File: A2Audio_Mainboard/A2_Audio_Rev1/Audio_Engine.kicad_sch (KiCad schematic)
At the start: 22 parts, among them U10 OPA1622IDRCR, U6 U_DAC_L, U7 U_DAC_R, U8 TPS7A2018PDBVR, U9 TPS7A2033PDBVR

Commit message: Added footprints and a few more parts.
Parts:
- C10, C100, C101, C102, C11, C12, C13, C14, C15, C7, C8, C9, C95, C96, C97, C98, C99: footprint (none) -> Capacitor_SMD:C_0402_1005Metric
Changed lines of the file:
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@@
 			)
 		)
-		(property "Footprint" ""
+		(property "Footprint" "Capacitor_SMD:C_0402_1005Metric"
 			(at 133.0452 99.06 0)
 			(hide yes)
@@
 			)
 		)
-		(property "Footprint" ""
+		(property "Footprint" "Capacitor_SMD:C_0402_1005Metric"
 			(at 179.07 56.1848 0)
 			(hide yes)
@@
 			)
 		)
-		(property "Footprint" ""
+		(property "Footprint" "Capacitor_SMD:C_0402_1005Metric"
 			(at 218.1352 186.69 0)
 			(hide yes)
@@
 			)
 		)
-		(property "Footprint" ""
+		(property "Footprint" "Capacitor_SMD:C_0402_1005Metric"
 			(at 28.9052 73.66 0)
 			(hide yes)
@@
 			)
 		)
-		(property "Footprint" ""
+		(property "Footprint" "Capacitor_SMD:C_0402_1005Metric"
 			(at 120.3452 97.79 0)
 			(hide yes)
@@
 			)
 		)
-		(property "Footprint" ""
+		(property "Footprint" "Capacitor_SMD:C_0402_1005Metric"
 			(at 34.29 29.5148 0)
 			(hide yes)
@@
 			)
 		)
-		(property "Footprint" ""
+		(property "Footprint" "Capacitor_SMD:C_0402_1005Metric"
 			(at 263.8552 97.79 0)
 			(hide yes)
@@
 			)
 		)
-		(property "Footprint" ""
+		(property "Footprint" "Capacitor_SMD:C_0402_1005Metric"
 			(at 36.5252 87.63 0)
 			(hide yes)
@@
 			)
 		)
-		(property "Footprint" ""
+		(property "Footprint" "Capacitor_SMD:C_0402_1005Metric"
 			(at 113.9952 102.87 0)
 			(hide yes)
@@
 			)
 		)
-		(property "Footprint" ""
+		(property "Footprint" "Capacitor_SMD:C_0402_1005Metric"
 			(at 33.02 56.1848 0)
 			(hide yes)
@@
 			)
 		)
-		(property "Footprint" ""
+		(property "Footprint" "Capacitor_SMD:C_0402_1005Metric"
 			(at 169.8752 85.09 0)
 			(hide yes)
@@
 			)
 		)
-		(property "Footprint" ""
+		(property "Footprint" "Capacitor_SMD:C_0402_1005Metric"
 			(at 203.5048 115.57 0)
 			(hide yes)
@@
 			)
 		)
-		(property "Footprint" ""
+		(property "Footprint" "Capacitor_SMD:C_0402_1005Metric"
 			(at 276.5552 99.06 0)
 			(hide yes)
@@
 			)
 		)
-		(property "Footprint" ""
+		(property "Footprint" "Capacitor_SMD:C_0402_1005Metric"
 			(at 257.5052 105.41 0)
 			(hide yes)
@@
 			)
 		)
-		(property "Footprint" ""
+		(property "Footprint" "Capacitor_SMD:C_0402_1005Metric"
 			(at 263.1948 113.03 0)
 			(hide yes)
@@
 			)
 		)
-		(property "Footprint" ""
+		(property "Footprint" "Capacitor_SMD:C_0402_1005Metric"
 			(at 180.0352 87.63 0)
 			(hide yes)
@@
 			)
 		)
-		(property "Footprint" ""
+		(property "Footprint" "Capacitor_SMD:C_0402_1005Metric"
 			(at 177.8 34.5948 0)
 			(hide yes)

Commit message: Refining of logic and adding battery connector
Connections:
- net 1V8_DIG: no longer C9.1, U10.8 (EN), U6.25 (VCP), U6.26 (VP), U6.31 (VL), U6.7 (VA), U7.25 (VCP), U7.26 (VP), U7.30 (ADR), U7.31 (VL), U7.7 (VA), U9.5 (OUT)
- new net 3V3_ANA: C9.1, U10.8 (EN), U6.25 (VCP), U6.26 (VP), U6.31 (VL), U6.7 (VA), U7.25 (VCP), U7.26 (VP), U7.30 (ADR), U7.31 (VL), U7.7 (VA), U9.5 (OUT)
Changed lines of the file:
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@@
-	)
-	(junction
-		(at 267.97 77.47)
-		(diameter 0)
-		(color 0 0 0 0)
 	)
 	(junction
@@
 	(wire
 		(pts
-			(xy 251.46 77.47) (xy 267.97 77.47)
-		)
-		(stroke
-			(width 0)
-			(type default)
-		)
-	)
-	(wire
-		(pts
 			(xy 410.21 130.81) (xy 417.83 130.81)
 		)
@@
 	(wire
 		(pts
+			(xy 251.46 77.47) (xy 255.27 77.47)
+		)
+		(stroke
+			(width 0)
+			(type default)
+		)
+	)
+	(wire
+		(pts
 			(xy 107.95 49.53) (xy 154.94 49.53)
 		)
@@
 	(wire
 		(pts
-			(xy 267.97 77.47) (xy 267.97 82.55)
-		)
-		(stroke
-			(width 0)
-			(type default)
-		)
-	)
-	(wire
-		(pts
 			(xy 185.42 40.64) (xy 185.42 35.56)
 		)
@@
 	(wire
 		(pts
-			(xy 267.97 76.2) (xy 267.97 77.47)
-		)
-		(stroke
+			(xy 267.97 76.2) (xy 267.97 82.55)
+		)
+		(stroke

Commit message: Fixing ERC errors
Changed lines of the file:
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@@
-		)
-	)
-	(wire
-		(pts
-			(xy 361.95 138.43) (xy 361.95 139.7)
-		)
-		(stroke
-			(width 0)
-			(type default)
 		)
 	)
@@
 	)
 	(label "3V3_ANA"
-		(at 271.78 76.2 0)
+		(at 284.48 76.2 0)
 		(effects
 			(font
@@
 	)
 	(label "AUDIO_OUT_L"
-		(at 359.41 125.73 0)
+		(at 356.87 125.73 0)
 		(effects
 			(font
@@
 	)
 	(label "AUDIO_OUT_R"
-		(at 359.41 133.35 0)
+		(at 356.87 133.35 0)
 		(effects
 			(font
@@
 	)
 	(label "3V3_ANA"
-		(at 119.38 95.25 0)
+		(at 130.81 95.25 0)
 		(effects
 			(font
@@
 	)
 	(label "3V3_ANA"
-		(at 364.49 138.43 0)
+		(at 361.95 138.43 0)
 		(effects
 			(font
@@
 	)
 	(label "1V8_DIG"
-		(at 111.76 77.47 0)
+		(at 124.46 77.47 0)
 		(effects
 			(font

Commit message: Fixed even more schematic errors
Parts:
- added R19, R31: 4.7kΩ, Resistor_SMD:R_0402_1005Metric, symbol symbols:R
- C10, C13: value 2.2µF -> 4.7µF
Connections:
- net 3V3_ANA: now also R19.2, R31.2
- net I2C_DAC_SCL: now also R19.1
- net I2C_DAC_SDA: now also R31.1
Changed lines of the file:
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@@
 	)
 	(junction
+		(at 153.67 111.76)
+		(diameter 0)
+		(color 0 0 0 0)
+	)
+	(junction
 		(at 260.35 71.12)
 		(diameter 0)
@@
 	)
 	(junction
+		(at 144.78 49.53)
+		(diameter 0)
+		(color 0 0 0 0)
+	)
+	(junction
 		(at 185.42 64.77)
 		(diameter 0)
@@
 	(wire
 		(pts
+			(xy 134.62 121.92) (xy 153.67 121.92)
+		)
+		(stroke
+			(width 0)
+			(type default)
+		)
+	)
+	(wire
+		(pts
 			(xy 154.94 31.75) (xy 257.81 31.75)
 		)
@@
 	(wire
 		(pts
+			(xy 144.78 49.53) (xy 144.78 123.19)
+		)
+		(stroke
+			(width 0)
+			(type default)
+		)
+	)
+	(wire
+		(pts
 			(xy 203.2 157.48) (xy 203.2 190.5)
 		)
@@
 	(wire
 		(pts
-			(xy 107.95 49.53) (xy 154.94 49.53)
+			(xy 107.95 49.53) (xy 144.78 49.53)
 		)
 		(stroke
@@
 	(wire
 		(pts
-			(xy 24.13 111.76) (xy 158.75 111.76)
+			(xy 24.13 111.76) (xy 153.67 111.76)
 		)
 		(stroke
@@
 	(wire
 		(pts
+			(xy 153.67 121.92) (xy 153.67 111.76)
+		)
+		(stroke
+			(width 0)
+			(type default)
+		)
+	)
+	(wire
+		(pts
 			(xy 161.29 35.56) (xy 170.18 35.56)
 		)
@@
 	(wire
 		(pts
+			(xy 144.78 49.53) (xy 154.94 49.53)
+		)
+		(stroke
+			(width 0)
+			(type default)
+		)
+	)
+	(wire
+		(pts
 			(xy 171.45 58.42) (xy 184.15 58.42)
 		)
@@
 	(wire
 		(pts
+			(xy 153.67 111.76) (xy 158.75 111.76)
+		)
+		(stroke
+			(width 0)
+			(type default)
+		)
+	)
+	(wire
+		(pts
 			(xy 185.42 67.31) (xy 182.88 67.31)
 		)
@@
 		)
 	)
+	(label "3V3_ANA"
+		(at 134.62 129.54 0)
+		(effects
+			(font
+				(size 1.27 1.27)
+			)
+			(justify left bottom)
+		)
+	)
 	(label "1V8_DIG"
 		(at 255.27 77.47 0)
@@
 		)
 	)
+	(label "3V3_ANA"
+		(at 144.78 130.81 270)
+		(effects
+			(font
+				(size 1.27 1.27)
+			)
+			(justify right bottom)
+		)
+	)
 	(label "1V8_DIG"
 		(at 124.46 77.47 0)
@@
 			)
 		)
-		(property "Value" "2.2µF"
+		(property "Value" "4.7µF"
 			(at 30.48 25.4 90)
 			(show_name no)
@@
 	)
 	(symbol
+		(lib_id "symbols:R")
+		(at 144.78 127 0)
+		(unit 1)
+		(body_style 1)
+		(exclude_from_sim no)
+		(in_bom yes)
+		(on_board yes)
+		(in_pos_files yes)
+		(dnp no)
+		(fields_autoplaced yes)
+		(property "Reference" "R31"
+			(at 147.32 125.7299 0)
+			(show_name no)
+			(do_not_autoplace no)
+			(effects
+				(font
+					(size 1.27 1.27)
+				)
+				(justify left)
+			)
+		)
+		(property "Value" "4.7kΩ"
+			(at 147.32 128.2699 0)
+			(show_name no)
+			(do_not_autoplace no)
+			(effects
+				(font
+					(size 1.27 1.27)
+				)
+				(justify left)
+			)
+		)
+		(property "Footprint" "Resistor_SMD:R_0402_1005Metric"
+			(at 143.002 127 90)
+			(hide yes)
+			(show_name no)
+			(do_not_autoplace no)
+			(effects
+				(font
+					(size 1.27 1.27)
+				)
+			)
+		)
+		(property "Datasheet" ""
+			(at 144.78 127 0)
+			(hide yes)
+			(show_name no)
+			(do_not_autoplace no)
+			(effects
+				(font
+					(size 1.27 1.27)
+				)
+			)
+		)
+		(property "Description" "Resistor"
+			(at 144.78 127 0)
+			(hide yes)
+			(show_name no)
+			(do_not_autoplace no)
+			(effects
+				(font
+					(size 1.27 1.27)
+				)
+			)
+		)
+		(pin "1"
+		)
+		(pin "2"
+		)
+		(instances
+			(project "A2_Audio_Rev1"
+				(path "/6bc02254-56bf-4f9a-8c1a-77c700c92092/966fe543-f3f2-44f2-9a96-3d2890d0362e"
+					(reference "R31")
+					(unit 1)
+				)
+			)
+		)
+	)
+	(symbol
 		(lib_id "symbols:GND")
 		(at 168.91 85.09 0)
@@
 	)
 	(symbol
+		(lib_id "symbols:R")
+		(at 134.62 125.73 0)
+		(unit 1)
+		(body_style 1)
+		(exclude_from_sim no)
+		(in_bom yes)
+		(on_board yes)
+		(in_pos_files yes)
+		(dnp no)
+		(fields_autoplaced yes)
+		(property "Reference" "R19"
+			(at 137.16 124.4599 0)
+			(show_name no)
+			(do_not_autoplace no)
+			(effects
+				(font
+					(size 1.27 1.27)
+				)
+				(justify left)
+			)
+		)
+		(property "Value" "4.7kΩ"
+			(at 137.16 126.9999 0)
+			(show_name no)
+			(do_not_autoplace no)
+			(effects
+				(font
+					(size 1.27 1.27)
+				)
+				(justify left)
+			)
+		)
+		(property "Footprint" "Resistor_SMD:R_0402_1005Metric"
+			(at 132.842 125.73 90)
+			(hide yes)
+			(show_name no)
+			(do_not_autoplace no)
+			(effects
+				(font
+					(size 1.27 1.27)
+				)
+			)
+		)
+		(property "Datasheet" ""
+			(at 134.62 125.73 0)
+			(hide yes)
+			(show_name no)
+			(do_not_autoplace no)
+			(effects
+				(font
+					(size 1.27 1.27)
+				)
+			)
+		)
+		(property "Description" "Resistor"
+			(at 134.62 125.73 0)
+			(hide yes)
+			(show_name no)
+			(do_not_autoplace no)
+			(effects
+				(font
+					(size 1.27 1.27)
+				)
+			)
+		)
+		(pin "1"
+		)
+		(pin "2"
+		)
+		(instances
+			(project "A2_Audio_Rev1"
+				(path "/6bc02254-56bf-4f9a-8c1a-77c700c92092/966fe543-f3f2-44f2-9a96-3d2890d0362e"
+					(reference "R19")
+					(unit 1)
+				)
+			)
+		)
+	)
+	(symbol
 		(lib_id "symbols:GND")
 		(at 217.17 186.69 0)
@@
 			)
 		)
-		(property "Value" "2.2µF"
+		(property "Value" "4.7µF"
 			(at 173.736 39.37 90)
 			(show_name no)

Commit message: Final touches in schematic
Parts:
- added R32, R57: 22Ω, Resistor_SMD:R_0402_1005Metric, symbol symbols:R
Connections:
- net I2S_MCLK: now also R32.2, R57.2; no longer U6.37 (XTI/MCLK), U7.37 (XTI/MCLK)
- new net: R32.1, U7.37 (XTI/MCLK)
- new net: R57.1, U6.37 (XTI/MCLK)
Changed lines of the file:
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@@
 	(wire
 		(pts
-			(xy 280.67 54.61) (xy 251.46 54.61)
+			(xy 280.67 54.61) (xy 264.16 54.61)
 		)
 		(stroke
@@
 	(wire
 		(pts
-			(xy 113.03 54.61) (xy 113.03 20.32)
-		)
-		(stroke
-			(width 0)
-			(type default)
-		)
-	)
-	(wire
-		(pts
 			(xy 270.51 25.4) (xy 270.51 62.23)
 		)
@@
 	(wire
 		(pts
-			(xy 107.95 54.61) (xy 113.03 54.61)
+			(xy 107.95 54.61) (xy 109.22 54.61)
 		)
 		(stroke
@@
 	(wire
 		(pts
-			(xy 113.03 20.32) (xy 280.67 20.32)
-		)
-		(stroke
-			(width 0)
-			(type default)
-		)
-	)
-	(wire
-		(pts
 			(xy 176.53 102.87) (xy 267.97 102.87)
 		)
@@
 	(wire
 		(pts
+			(xy 116.84 20.32) (xy 280.67 20.32)
+		)
+		(stroke
+			(width 0)
+			(type default)
+		)
+	)
+	(wire
+		(pts
 			(xy 40.64 30.48) (xy 40.64 67.31)
 		)
@@
 	(wire
 		(pts
+			(xy 116.84 54.61) (xy 116.84 20.32)
+		)
+		(stroke
+			(width 0)
+			(type default)
+		)
+	)
+	(wire
+		(pts
 			(xy 245.11 190.5) (xy 271.78 190.5)
 		)
@@
 	(wire
 		(pts
+			(xy 256.54 54.61) (xy 251.46 54.61)
+		)
+		(stroke
+			(width 0)
+			(type default)
+		)
+	)
+	(wire
+		(pts
 			(xy 167.64 147.32) (xy 162.56 147.32)
 		)
@@
 	(hierarchical_label "I2S_MCLK"
 		(shape input)
-		(at 280.67 27.94 0)
+		(at 280.67 30.48 0)
 		(effects
 			(font
@@
 	)
 	(symbol
+		(lib_id "symbols:R")
+		(at 260.35 54.61 90)
+		(unit 1)
+		(body_style 1)
+		(exclude_from_sim no)
+		(in_bom yes)
+		(on_board yes)
+		(in_pos_files yes)
+		(dnp no)
+		(fields_autoplaced yes)
+		(property "Reference" "R32"
+			(at 260.35 48.26 90)
+			(show_name no)
+			(do_not_autoplace no)
+			(effects
+				(font
+					(size 1.27 1.27)
+				)
+			)
+		)
+		(property "Value" "22Ω"
+			(at 260.35 50.8 90)
+			(show_name no)
+			(do_not_autoplace no)
+			(effects
+				(font
+					(size 1.27 1.27)
+				)
+			)
+		)
+		(property "Footprint" "Resistor_SMD:R_0402_1005Metric"
+			(at 260.35 56.388 90)
+			(hide yes)
+			(show_name no)
+			(do_not_autoplace no)
+			(effects
+				(font
+					(size 1.27 1.27)
+				)
+			)
+		)
+		(property "Datasheet" ""
+			(at 260.35 54.61 0)
+			(hide yes)
+			(show_name no)
+			(do_not_autoplace no)
+			(effects
+				(font
+					(size 1.27 1.27)
+				)
+			)
+		)
+		(property "Description" "Resistor"
+			(at 260.35 54.61 0)
+			(hide yes)
+			(show_name no)
+			(do_not_autoplace no)
+			(effects
+				(font
+					(size 1.27 1.27)
+				)
+			)
+		)
+		(pin "1"
+		)
+		(pin "2"
+		)
+		(instances
+			(project "A2_Audio_Rev1"
+				(path "/6bc02254-56bf-4f9a-8c1a-77c700c92092/966fe543-f3f2-44f2-9a96-3d2890d0362e"
+					(reference "R32")
+					(unit 1)
+				)
+			)
+		)
+	)
+	(symbol
 		(lib_id "symbols:C")
 		(at 113.03 99.06 0)
@@
 					(unit 1)
 				)
+			)
+		)
+	)
+	(symbol
+		(lib_id "symbols:R")
+		(at 113.03 54.61 90)
+		(unit 1)
+		(body_style 1)
+		(exclude_from_sim no)
+		(in_bom yes)
+		(on_board yes)
+		(in_pos_files yes)
+		(dnp no)
+		(fields_autoplaced yes)
+		(property "Reference" "R57"
+			(at 113.03 48.26 90)
+			(show_name no)
+			(do_not_autoplace no)
+			(effects
+				(font
+					(size 1.27 1.27)
+				)
+			)
+		)
+		(property "Value" "22Ω"
+			(at 113.03 50.8 90)
+			(show_name no)
+			(do_not_autoplace no)
+			(effects
+				(font
+					(size 1.27 1.27)
+				)
+			)
+		)
+		(property "Footprint" "Resistor_SMD:R_0402_1005Metric"
+			(at 113.03 56.388 90)
+			(hide yes)
+			(show_name no)
+			(do_not_autoplace no)
+			(effects
+				(font
+					(size 1.27 1.27)
+				)
+			)
+		)
+		(property "Datasheet" ""
+			(at 113.03 54.61 0)
+			(hide yes)
+			(show_name no)
+			(do_not_autoplace no)
+			(effects
+				(font
+					(size 1.27 1.27)
+				)
+			)
+		)
+		(property "Description" "Resistor"
+			(at 113.03 54.61 0)
+			(hide yes)
+			(show_name no)
+			(do_not_autoplace no)
+			(effects
+				(font
+					(size 1.27 1.27)
+				)
+			)
+		)
+		(pin "1"
+		)
+		(pin "2"
+		)
+		(instances
+			(project "A2_Audio_Rev1"
+				(path "/6bc02254-56bf-4f9a-8c1a-77c700c92092/966fe543-f3f2-44f2-9a96-3d2890d0362e"
+					(reference "R57")
+					(unit 1)
+				)

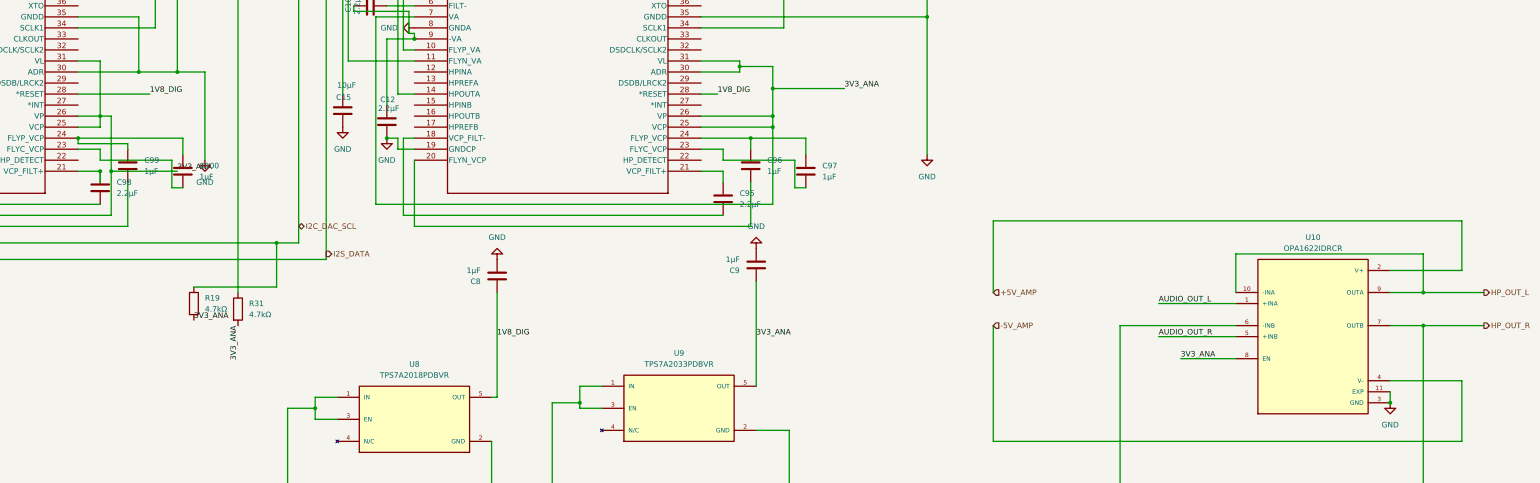
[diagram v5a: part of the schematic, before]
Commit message: Fixed SD Card logic and power error
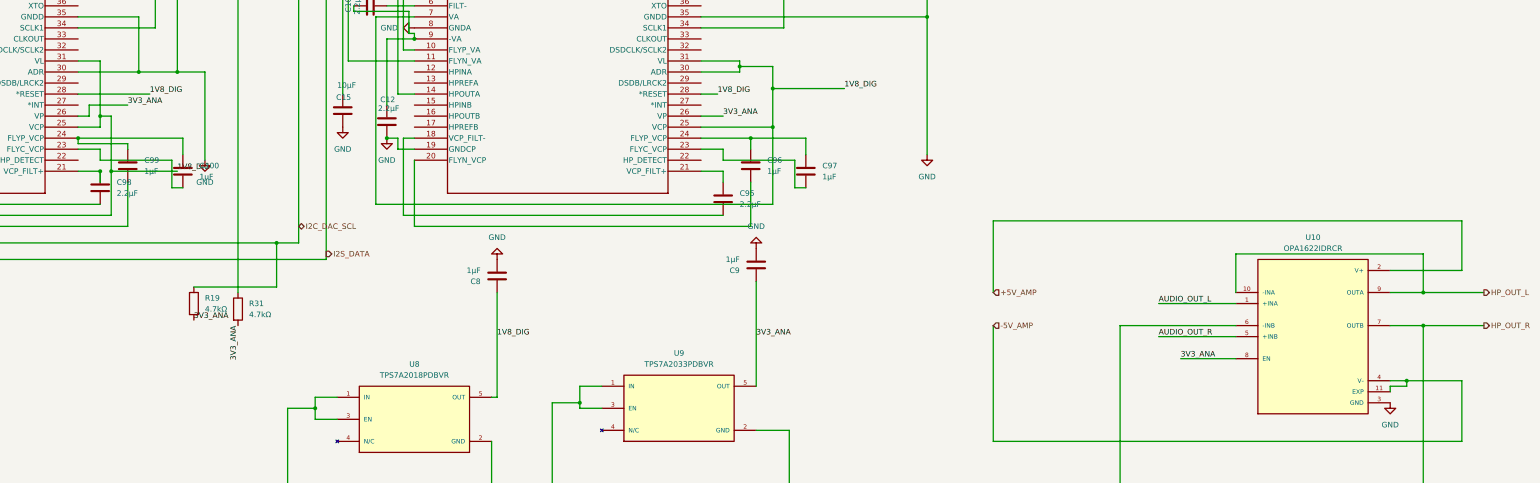
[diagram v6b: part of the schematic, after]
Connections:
- net -5V_AMP is gone; now on net EXP: U10.4 (V-)
- net 1V8_DIG: now also U6.25 (VCP), U6.31 (VL), U6.7 (VA), U7.25 (VCP), U7.30 (ADR), U7.31 (VL), U7.7 (VA)
- net 3V3_ANA: no longer U6.25 (VCP), U6.31 (VL), U6.7 (VA), U7.25 (VCP), U7.30 (ADR), U7.31 (VL), U7.7 (VA)
- net EXP: no longer C11.2, C12.2, C14.2, C15.2, C7.2, C8.2, C9.2, U10.3 (GND), U6.19 (GNDCP), U6.30 (ADR), U6.35 (GNDD), U6.41 (EPAD), U6.8 (GNDA), U7.19 (GNDCP), U7.35 (GNDD), U7.41 (EPAD), U7.8 (GNDA), U8.2 (GND), U9.2 (GND)
- new net GND: C11.2, C12.2, C14.2, C15.2, C7.2, C8.2, C9.2, U10.3 (GND), U6.19 (GNDCP), U6.30 (ADR), U6.35 (GNDD), U6.41 (EPAD), U6.8 (GNDA), U7.19 (GNDCP), U7.35 (GNDD), U7.41 (EPAD), U7.8 (GNDA), U8.2 (GND), U9.2 (GND)
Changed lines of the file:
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@@
+	)
+	(junction
+		(at 414.02 143.51)
+		(diameter 0)
+		(color 0 0 0 0)
 	)
 	(junction
@@
 	)
 	(junction
-		(at 267.97 82.55)
-		(diameter 0)
-		(color 0 0 0 0)
-	)
-	(junction
 		(at 121.92 72.39)
 		(diameter 0)
@@
 	)
 	(junction
-		(at 410.21 148.59)
-		(diameter 0)
-		(color 0 0 0 0)
-	)
-	(junction
 		(at 41.91 64.77)
 		(diameter 0)
@@
 	(wire
 		(pts
+			(xy 110.49 82.55) (xy 110.49 80.01)
+		)
+		(stroke
+			(width 0)
+			(type default)
+		)
+	)
+	(wire
+		(pts
 			(xy 115.57 95.25) (xy 130.81 95.25)
 		)
@@
 	(wire
 		(pts
+			(xy 251.46 82.55) (xy 256.54 82.55)
+		)
+		(stroke
+			(width 0)
+			(type default)
+		)
+	)
+	(wire
+		(pts
 			(xy 107.95 69.85) (xy 113.03 69.85)
 		)
@@
 	(wire
 		(pts
-			(xy 251.46 82.55) (xy 267.97 82.55)
-		)
-		(stroke
-			(width 0)
-			(type default)
-		)
-	)
-	(wire
-		(pts
 			(xy 21.59 30.48) (xy 26.67 30.48)
 		)
@@
 	(wire
 		(pts
+			(xy 410.21 146.05) (xy 410.21 144.78)
+		)
+		(stroke
+			(width 0)
+			(type default)
+		)
+	)
+	(wire
+		(pts
 			(xy 107.95 49.53) (xy 144.78 49.53)
 		)
@@
 	(wire
 		(pts
-			(xy 267.97 82.55) (xy 267.97 85.09)
+			(xy 267.97 76.2) (xy 267.97 85.09)
 		)
 		(stroke
@@
 	(wire
 		(pts
+			(xy 414.02 143.51) (xy 410.21 143.51)
+		)
+		(stroke
+			(width 0)
+			(type default)
+		)
+	)
+	(wire
+		(pts
 			(xy 24.13 111.76) (xy 153.67 111.76)
 		)
@@
 	(wire
 		(pts
+			(xy 110.49 80.01) (xy 119.38 80.01)
+		)
+		(stroke
+			(width 0)
+			(type default)
+		)
+	)
+	(wire
+		(pts
 			(xy 41.91 69.85) (xy 38.1 69.85)
 		)
@@
 	(wire
 		(pts
-			(xy 107.95 82.55) (xy 113.03 82.55)
+			(xy 410.21 144.78) (xy 414.02 144.78)
+		)
+		(stroke
+			(width 0)
+			(type default)
+		)
+	)
+	(wire
+		(pts
+			(xy 107.95 82.55) (xy 110.49 82.55)
 		)
 		(stroke
@@
 	(wire
 		(pts
-			(xy 426.72 143.51) (xy 410.21 143.51)
+			(xy 426.72 143.51) (xy 414.02 143.51)
 		)
 		(stroke
@@
 	(wire
 		(pts
+			(xy 414.02 144.78) (xy 414.02 143.51)
+		)
+		(stroke
+			(width 0)
+			(type default)
+		)
+	)
+	(wire
+		(pts
 			(xy 417.83 114.3) (xy 374.65 114.3)
 		)
@@
 	(wire
 		(pts
-			(xy 410.21 146.05) (xy 410.21 148.59)
-		)
-		(stroke
-			(width 0)
-			(type default)
-		)
-	)
-	(wire
-		(pts
 			(xy 25.4 58.42) (xy 39.37 58.42)
 		)
@@
 		(pts
 			(xy 31.75 105.41) (xy 31.75 59.69)
-		)
-		(stroke
-			(width 0)
-			(type default)
-		)
-	)
-	(wire
-		(pts
-			(xy 267.97 76.2) (xy 267.97 82.55)
 		)
 		(stroke
@@
 	)
 	(label "3V3_ANA"
+		(at 256.54 82.55 0)
+		(effects
+			(font
+				(size 1.27 1.27)
+			)
+			(justify left bottom)
+		)
+	)
+	(label "1V8_DIG"
 		(at 284.48 76.2 0)
 		(effects
@@
 	)
 	(label "3V3_ANA"
-		(at 130.81 95.25 0)
+		(at 119.38 80.01 0)
 		(effects
 			(font
@@
 		(effects
 			(font
+				(size 1.27 1.27)
+			)
+			(justify left bottom)
+		)
+	)
+	(label "1V8_DIG"
+		(at 130.81 95.25 0)
+		(effects
+			(font
